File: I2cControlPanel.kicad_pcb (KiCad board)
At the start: 2 copper layers, 100 x 100 mm, 49 parts, among them J1 Conn_01x08, J2 Conn_01x06, J3 Conn_01x04, J4 Conn_01x04, J5 Conn_01x08, J6 Conn_01x04, SW1 SW_Push, SW2 SW_Push, SW3 SW_Push, SW4 SW_Push, SW5 SlideSwitch, U1 LP2985-3.3, U2 ATmega328PB-MU, U3 AQM0802

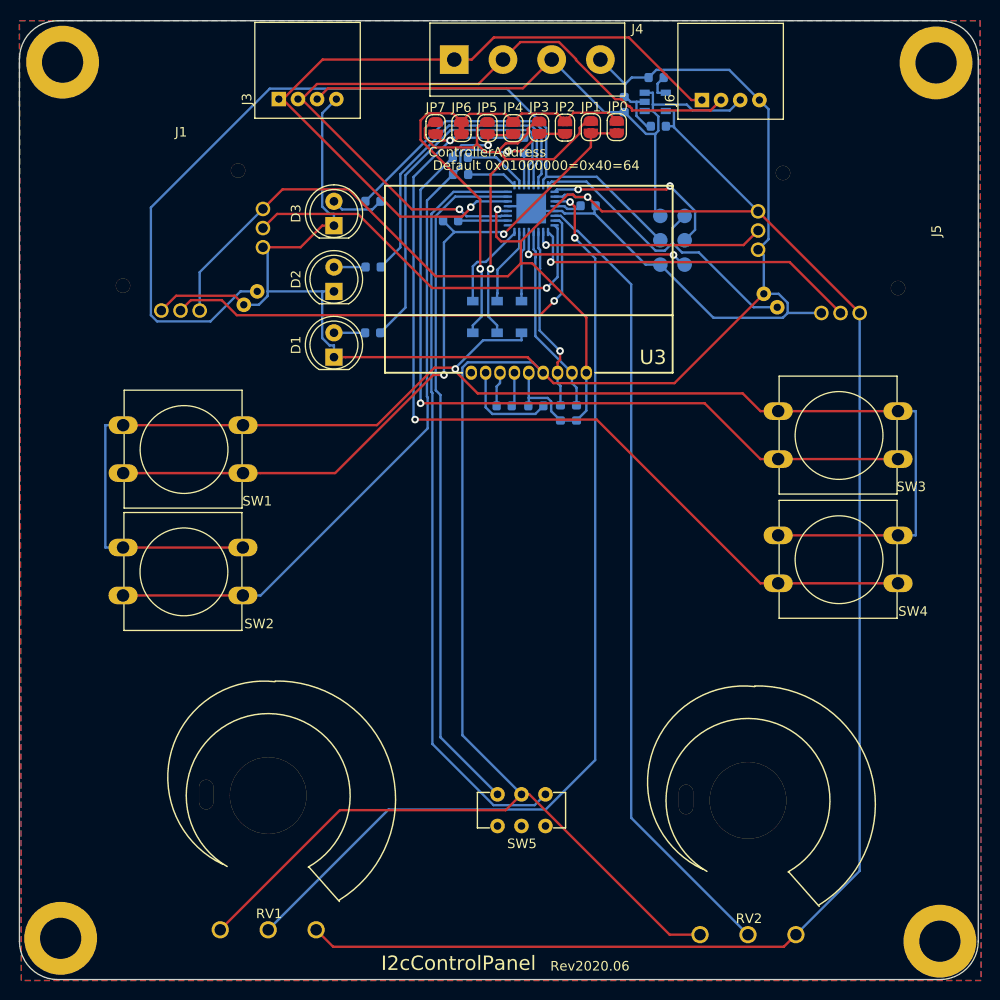
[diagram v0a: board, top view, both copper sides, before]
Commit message: Update for rev 2020.08
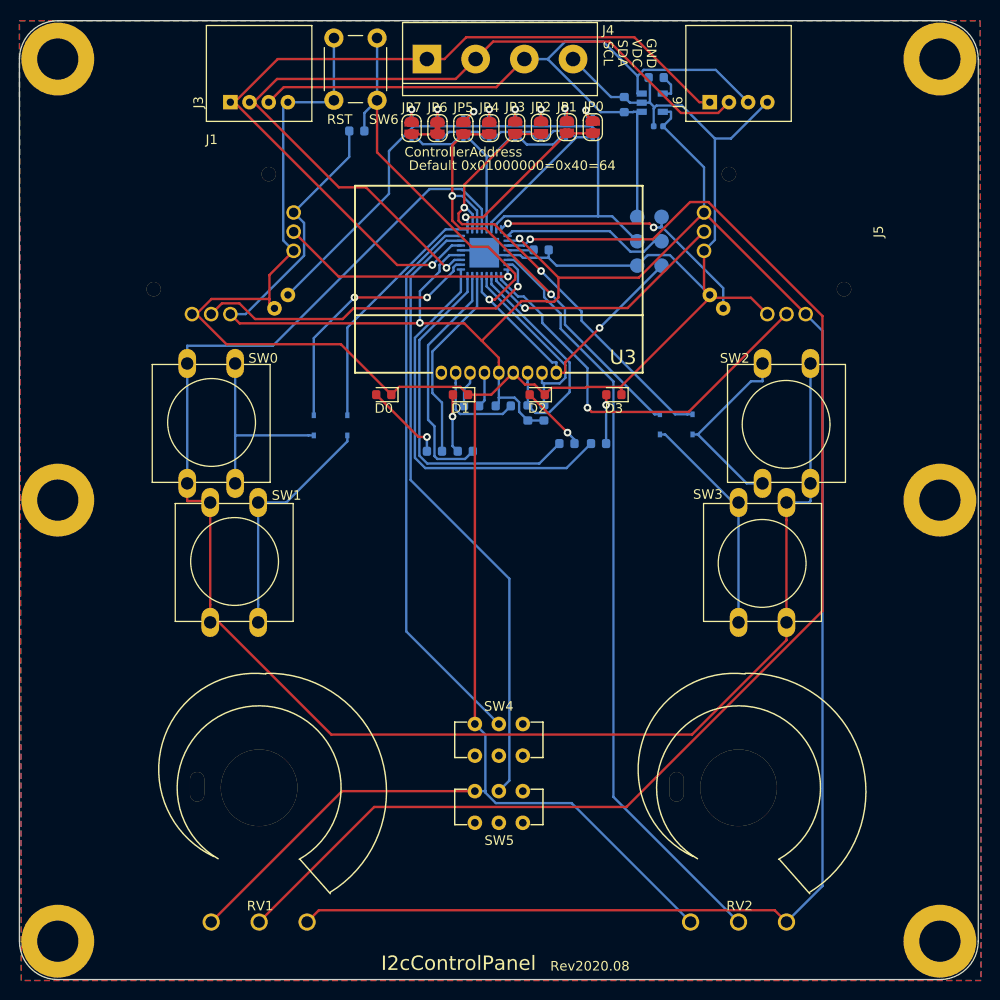
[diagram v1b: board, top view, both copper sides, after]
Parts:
- removed R8, R9: 10k, Resistor_SMD:R_0603_1608Metric
- added D10: D, Diode_SMD:D_SOD-323, B.Cu at (107.0, 61.1)
- added D11: D, Diode_SMD:D_SOD-323, B.Cu at (109.8, 61.1)
- added D12: D, Diode_SMD:D_SOD-323, B.Cu at (80.7, 92.2)
- added D13: D, Diode_SMD:D_SOD-323, B.Cu at (84.2, 92.2)
- added D14: D, Diode_SMD:D_SOD-323, B.Cu at (120.2, 92.1)
- added D15: D, Diode_SMD:D_SOD-323, B.Cu at (116.8, 92.1)
- added D3: LED3, Diode_SMD:D_0603_1608Metric, F.Cu at (112.0, 89.0)
- added D7: D, Diode_SMD:D_SOD-323, B.Cu at (99.0, 61.2)
- added D8: D, Diode_SMD:D_SOD-323, B.Cu at (101.7, 61.2)
- added D9: D, Diode_SMD:D_SOD-323, B.Cu at (104.4, 61.2)
- added REF5: MountingHole_4.3mm_M4_ISO7380_Pad, MountingHole:MountingHole_4.3mm_M4_ISO7380_Pad, F.Cu at (54.0, 100.0)
- added REF6: MountingHole_4.3mm_M4_ISO7380_Pad, MountingHole:MountingHole_4.3mm_M4_ISO7380_Pad, F.Cu at (146.0, 100.0)
- added SW4: SlideSwitch, my-kicad-footprints:SlideSwitch, F.Cu at (100.0, 125.0)
- added SW6: SW_Push, Button_Switch_THT:SW_PUSH_6mm, F.Cu at (87.3, 51.8)
- C1: value 1u -> 0.1u
- C3: value 2.2u -> 0.47u; footprint Capacitor_SMD:C_0603_1608Metric -> Capacitor_SMD:C_0402_1005Metric
- D0: renamed from D1; value LED_R -> LED0; footprint LED_THT:LED_D5.0mm -> Diode_SMD:D_0603_1608Metric
- D1: renamed from D2; value LED_Y -> LED1; footprint LED_THT:LED_D5.0mm -> Diode_SMD:D_0603_1608Metric
- D2: renamed from D3; value LED_G -> LED2; footprint LED_THT:LED_D5.0mm -> Diode_SMD:D_0603_1608Metric
- D4, D5, D6: footprint Diode_SMD:D_SOD-123 -> Diode_SMD:D_SOD-323
- R4: value 10k -> 1k
- U1: value LP2985-3.3 -> NJM12888F33
- moved R3 32.4 mm to (107.1, 94.1)
- moved R4 27.9 mm to (110.4, 94.1)
- moved D2 27.6 mm to (104.0, 89.0), turned to 180 degrees
- moved D4 22.8 mm to (90.9, 61.2)
- moved R2 21.5 mm to (96.5, 94.9)
- moved D5 20.7 mm to (93.6, 61.2)
- moved D6 19.7 mm to (96.3, 61.2)
- moved D1 17.0 mm to (96.0, 89.0), turned to 180 degrees
- moved R1 13.9 mm to (93.3, 94.9)
- moved R7 11.7 mm to (85.2, 61.5)
- moved SW3 7.89 mm to (127.5, 106.5), turned to 270 degrees
- moved U2 6.72 mm to (98.5, 74.2)
- moved C4 6.72 mm to (104.4, 73.9)
- moved D0 6.50 mm to (88.0, 89.0), turned to 180 degrees
- moved J5 5.64 mm to (130.0, 72.0)
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- renumbered SW1 to SW0, SW2 to SW1, SW3 to SW2, SW4 to SW3
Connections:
- D6 pad 1: /BtnSig3 -> /BtnSig1
- JP0 pad 2: /BtnSig3 -> Net-(D11-Pad2)
- JP1 pad 2: /BtnSig2 -> Net-(D10-Pad2)
- JP2 pad 2: /BtnSig3 -> Net-(D9-Pad2)
- JP3 pad 2: /BtnSig2 -> Net-(D8-Pad2)
- JP4 pad 2: /BtnSig3 -> Net-(D7-Pad2)
- JP5 pad 2: /BtnSig2 -> Net-(D6-Pad2)
- JP6 pad 2: /BtnSig3 -> Net-(D5-Pad2)
- JP7 pad 2: /BtnSig2 -> Net-(D4-Pad2)
- R1 pad 1: /LED_R -> /LED0
- R2 pad 1: /LED_Y -> /LED1
- R3 pad 1: /LED_G -> /LED2
- R4 pad 1: /BTN1 -> /LED3
- R4 pad 2: Net-(R4-Pad2) -> Net-(D3-Pad2)
- R7 pad 1: /BTN2 -> +3V3
- R7 pad 2: Net-(R7-Pad2) -> /RST
- SW0 pad 1: /BtnSig1 -> /BtnSig0
- SW0 pad 2: /BTN1 -> Net-(D12-Pad1)
- SW1 pad 1: /BtnSig1 -> /BtnSig0
- SW1 pad 2: /BTN2 -> Net-(D13-Pad1)
- SW2 pad 1: /BtnSig1 -> /BtnSig0
- SW2 pad 2: /BTN3 -> Net-(D14-Pad1)
- SW3 pad 1: /BtnSig1 -> /BtnSig0
- SW3 pad 2: /BTN4 -> Net-(D15-Pad1)
- SW5 pad 1: /Slide1 -> GND
- SW5 pad 2: GND -> /Slide1
- SW5 pad 3: /Slide2 -> Net-(SW5-Pad3)
- U2 pad 1: Net-(U2-Pad1) -> /LED3
- U2 pad 10: Net-(R8-Pad2) -> /BTN2
- U2 pad 11: Net-(R9-Pad2) -> /BTN3
- U2 pad 12: /LED_R -> /BtnSig0
- U2 pad 13: /LED_Y -> /BtnSig1
- U2 pad 14: /LED_G -> /BtnSig2
- U2 pad 2: Net-(R4-Pad2) -> /BTN0
- U2 pad 30: Net-(D4-Pad2) -> /LED0
- U2 pad 31: Net-(D5-Pad2) -> /LED1
- U2 pad 32: Net-(D6-Pad2) -> /LED2
- U2 pad 9: Net-(R7-Pad2) -> /BTN1
- U3 pad 9: +3V3 -> /RST
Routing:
- net /BtnSig0: track 0.00 -> 172.3 mm
- net /BtnSig1: track 152.4 -> 26.4 mm, vias 1 -> 0
- net /BTN4: track 99.2 -> 2.70 mm, vias 2 -> 0
- net /RST: track 19.1 -> 69.3 mm
- net /BtnSig3: track 48.4 -> 0.00 mm, vias 1 -> 0
- net /LED3: track 0.00 -> 41.5 mm
- net /Rotery1: track 102.4 -> 142.6 mm, vias 2 -> 1
- net /BTN3: track 87.5 -> 48.4 mm
- net /LED_R: track 38.4 -> 0.00 mm
- net /LED2: track 0.00 -> 36.6 mm
- net /LED_Y: track 32.9 -> 0.00 mm
- net /BTN1: track 76.9 -> 44.1 mm, vias 2 -> 1
- net /BTN2: track 81.2 -> 50.3 mm, vias 1 -> 2
- net /LED_G: track 28.1 -> 0.00 mm
- net /BTN0: track 0.00 -> 26.8 mm, vias 0 -> 2
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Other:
- board text added: "GND"
- board text added: "RST"
- board text added: "Rev2020.08"
- board text added: "SCL"
- board text added: "SDA"
- board text added: "VDC"
- board text removed: "Rev2020.06"

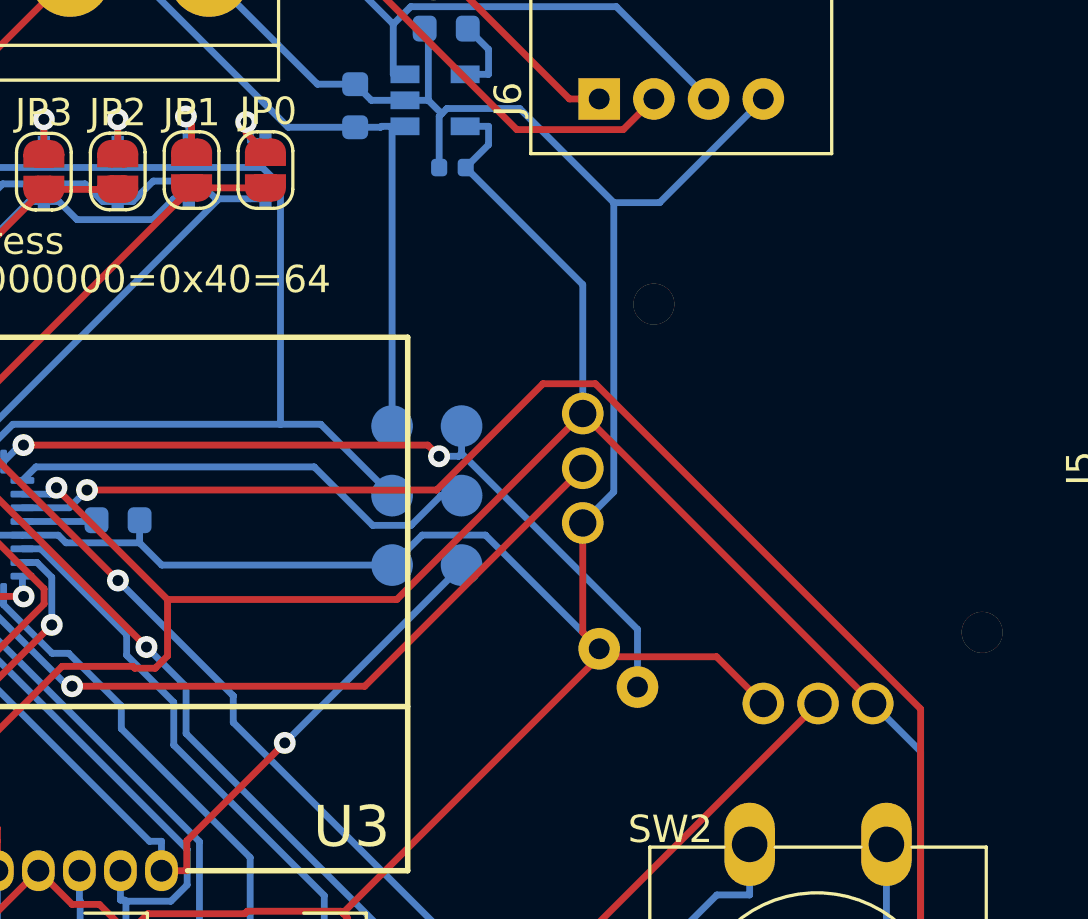
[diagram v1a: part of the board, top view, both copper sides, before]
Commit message: Replace gnd and 3v3 for right joy stick
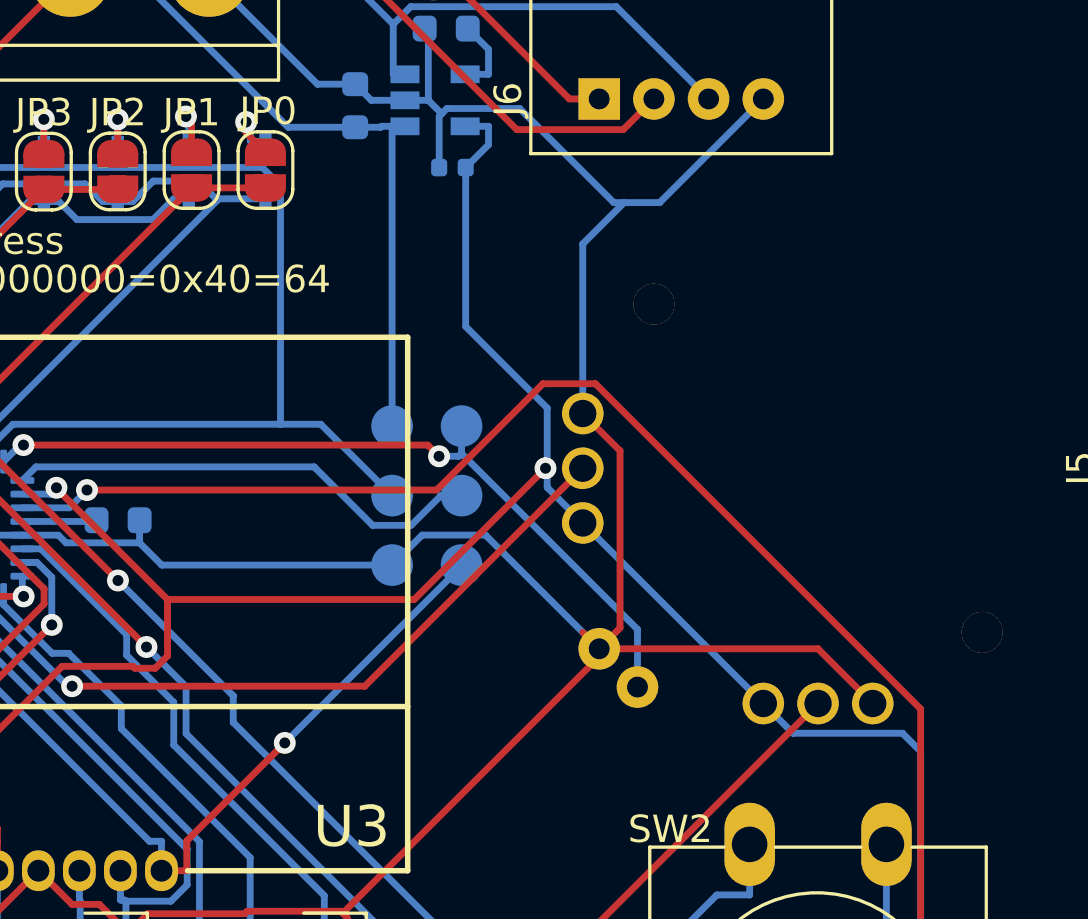
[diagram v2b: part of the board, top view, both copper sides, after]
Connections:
- J5 pad 1: +3V3 -> GND
- J5 pad 3: GND -> +3V3
- J5 pad 4: GND -> +3V3
- J5 pad 6: +3V3 -> GND
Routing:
- net GND: track 295.2 -> 300.9 mm
- net +3V3: track 259.2 -> 259.4 mm, vias 2 -> 3

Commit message: Update footprint of volume
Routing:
- net +3V3: track 259.4 -> 258.4 mm
- net /Rotery2: track 79.4 -> 78.4 mm

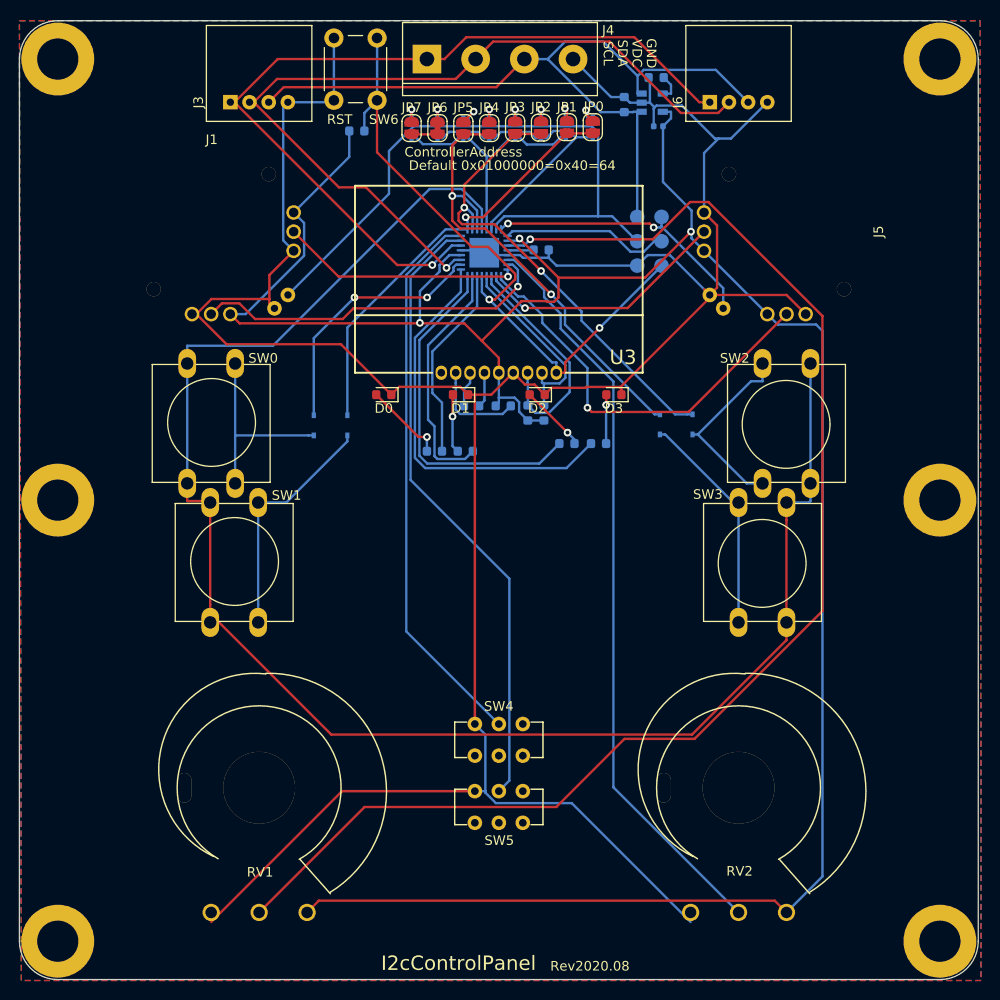
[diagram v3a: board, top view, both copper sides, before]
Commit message: Correct button line for address pads
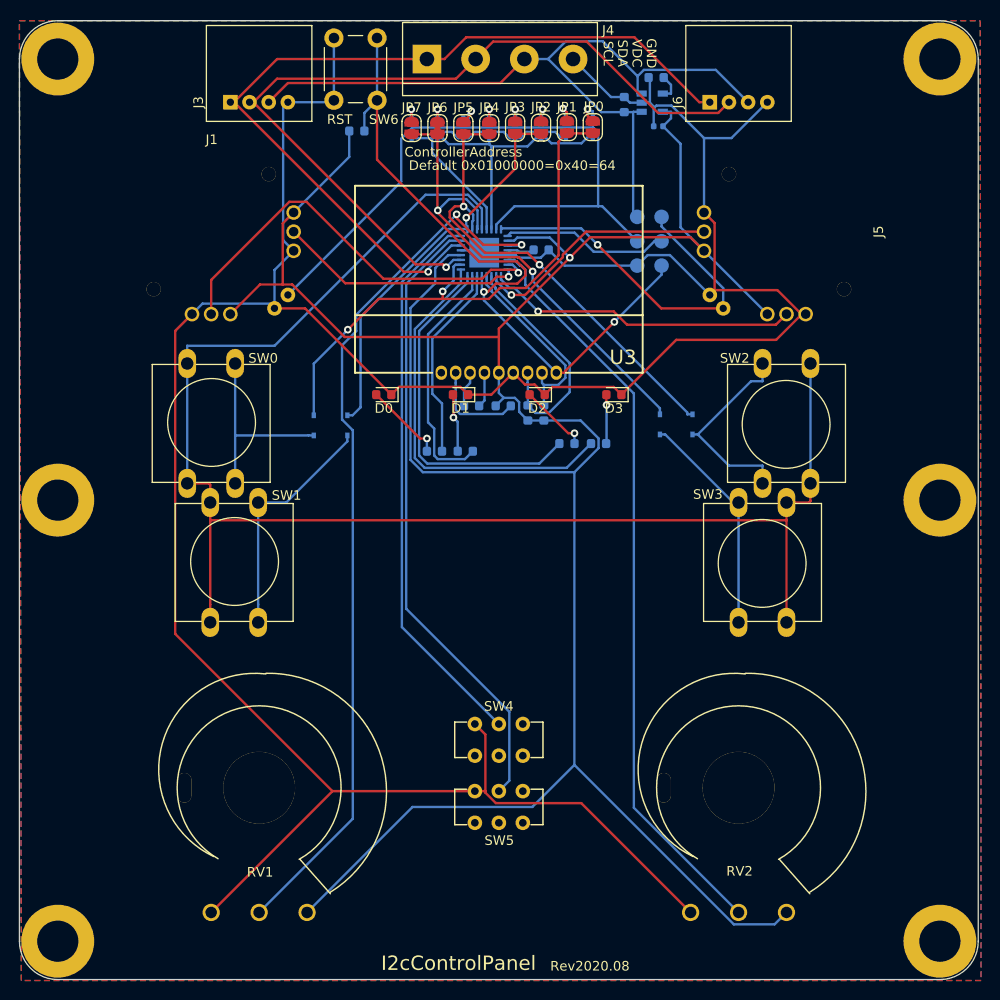
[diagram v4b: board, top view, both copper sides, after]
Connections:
- JP0 pad 1: /BTN1 -> /BTN0
- JP1 pad 1: /BTN1 -> /BTN0
- JP2 pad 1: /BTN2 -> /BTN1
- JP3 pad 1: /BTN2 -> /BTN1
- JP4 pad 1: /BTN3 -> /BTN2
- JP5 pad 1: /BTN3 -> /BTN2
- JP6 pad 1: /BTN4 -> /BTN3
- JP7 pad 1: /BTN4 -> /BTN3
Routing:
- net /Rotery1: track 142.2 -> 92.1 mm, vias 1 -> 2
- net /BTN0: track 26.8 -> 56.1 mm
- net GND: track 300.9 -> 321.2 mm
- net +3V3: track 258.4 -> 272.3 mm, vias 3 -> 1
- net /BtnSig0: track 172.3 -> 160.7 mm
- net /HoriValueR: track 43.0 -> 32.5 mm
- net /JoyBtnR: track 29.4 -> 38.9 mm, vias 2 -> 1
- net /HoriValueL: track 37.6 -> 44.4 mm
- net /BtnSig2: track 31.1 -> 26.7 mm
- net /BtnSig1: track 26.4 -> 29.8 mm
- net /BTN1: track 44.1 -> 40.8 mm
- net /BTN4: track 2.70 -> 0.00 mm
- net /RST: track 69.3 -> 71.8 mm
- net /BTN3: track 48.4 -> 50.9 mm
- net Net-(D14-Pad1): track 20.3 -> 21.4 mm
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
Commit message: Update slide switch position and labels for each buttons
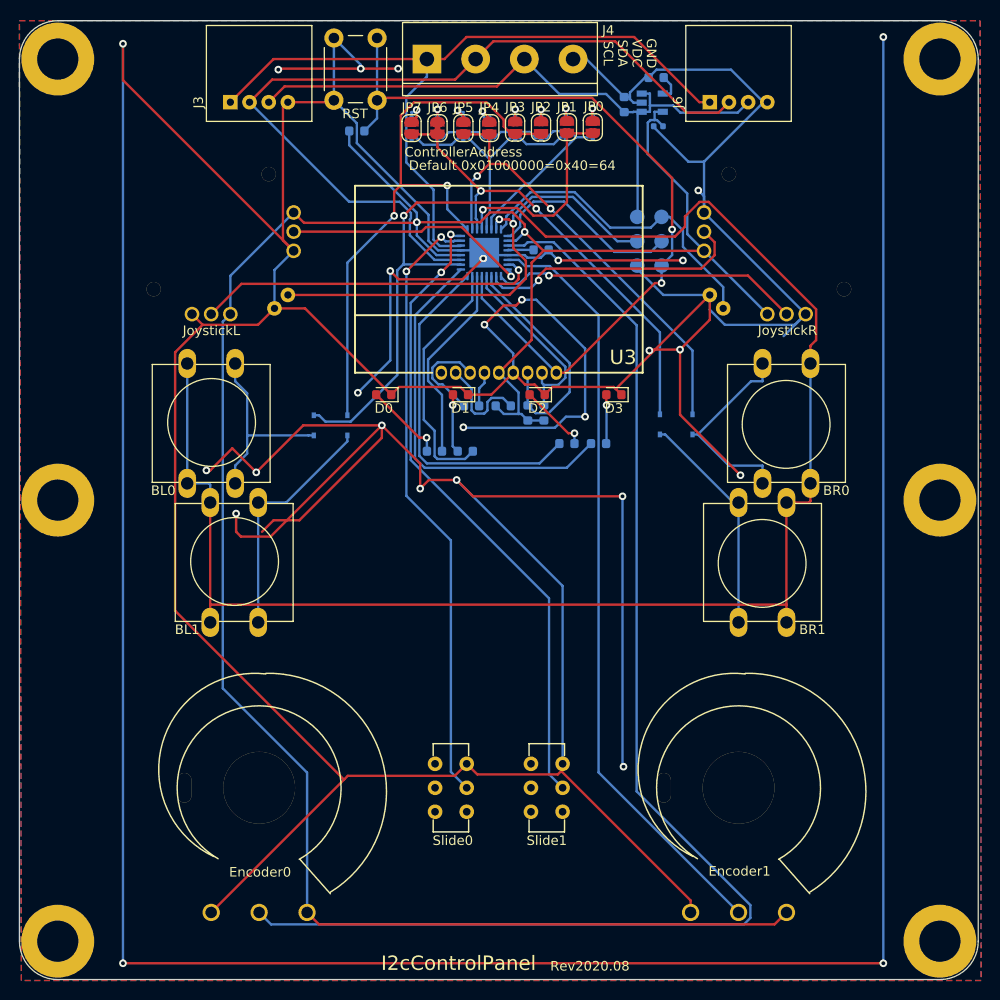
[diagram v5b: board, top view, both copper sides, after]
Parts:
- J1: value Conn_01x08 -> JoystickL
- J5: value Conn_01x08 -> JoystickR
- moved Slide1 7.07 mm to (105.0, 130.0), turned to 270 degrees
- moved Slide0 5.39 mm to (95.0, 130.0), turned to 270 degrees
- renumbered SW0 to BL0, SW1 to BL1, SW2 to BR0, SW3 to BR1, RV1 to Encoder0, RV2 to Encoder1, SW5 to Slide0, SW4 to Slide1
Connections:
- Slide0 pad 2: /Slide1 -> /Slide0
- Slide1 pad 2: /Slide2 -> /Slide1
- U2 pad 7: /Slide1 -> /Slide0
- U2 pad 8: /Slide2 -> /Slide1
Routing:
- net GND: track 321.2 -> 923.1 mm, vias 0 -> 28
- net /Slide0: track 0.00 -> 63.8 mm, vias 0 -> 2
- net /Slide2: track 58.4 -> 0.00 mm
- net /Rotery1: track 92.1 -> 135.9 mm, vias 2 -> 0
- net /BTN1: track 40.8 -> 61.0 mm, vias 1 -> 2
- net +3V3: track 272.3 -> 252.2 mm, vias 1 -> 2
- net /JoyBtnL: track 67.6 -> 51.1 mm, vias 0 -> 2
- net VDC: track 81.2 -> 68.7 mm
- net /RST: track 71.8 -> 84.1 mm
- net /BtnSig0: track 160.7 -> 169.6 mm, vias 0 -> 1
- net /HoriValueL: track 44.4 -> 35.9 mm
- net /SCL: track 87.9 -> 79.7 mm, vias 1 -> 0
- net Net-(C6-Pad2): track 3.72 -> 10.2 mm
- net /BTN0: track 56.1 -> 62.5 mm, vias 2 -> 1
- net /JoyBtnR: track 38.9 -> 33.5 mm, vias 1 -> 0
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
